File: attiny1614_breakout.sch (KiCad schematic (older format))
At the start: 15 parts, among them J1 Conn_01x07, J2 Conn_01x07, J3 UPDI, SW1 Reset, U1 REG102-5, U2 ATtiny1614-SS

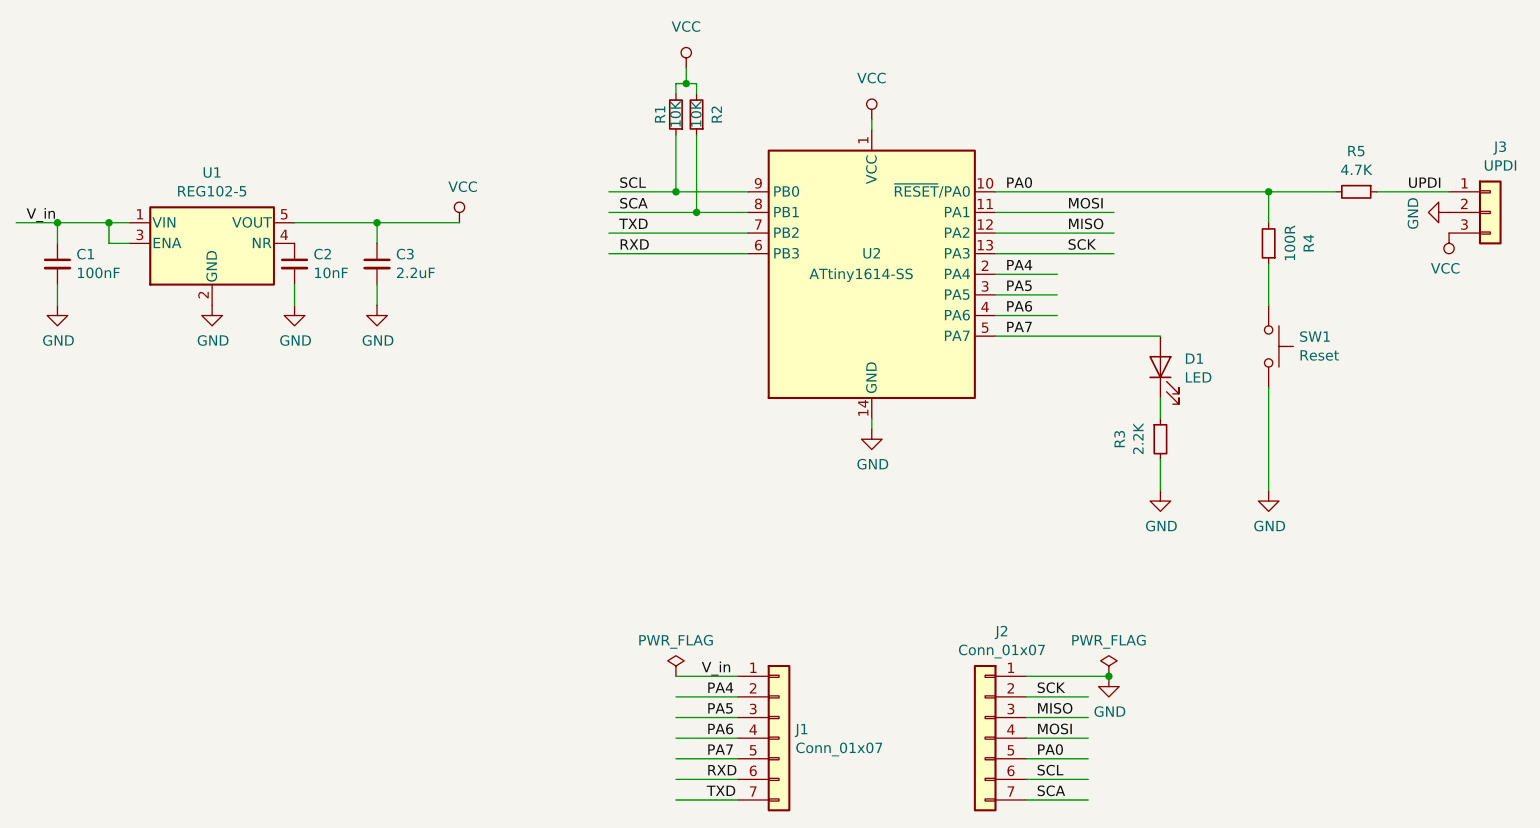
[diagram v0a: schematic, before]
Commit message: moved to programmer pin to Vin, fixed typos, added thermal relief
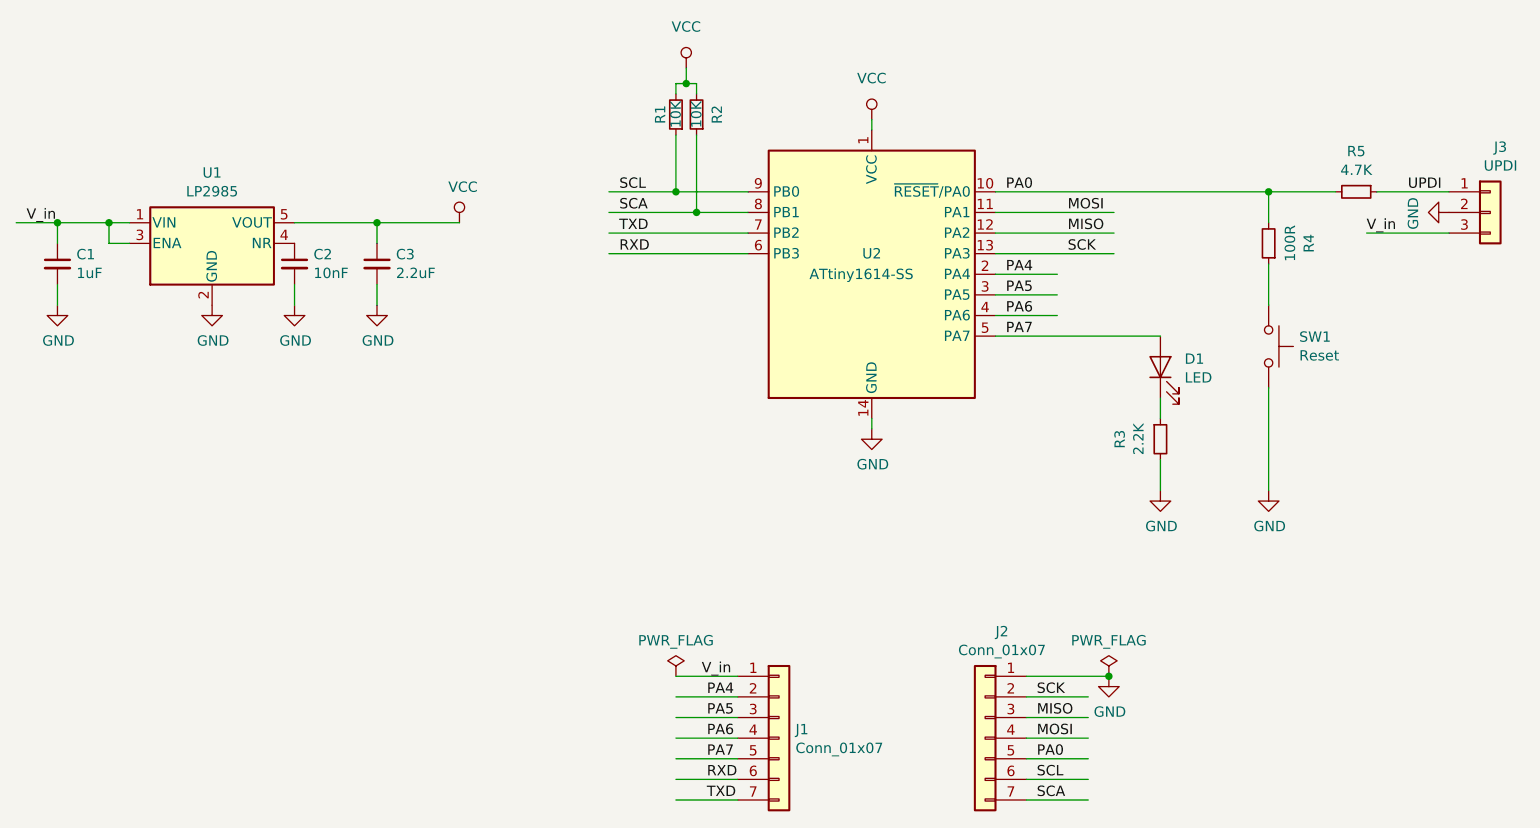
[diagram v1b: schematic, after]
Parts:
- C1: value 100nF -> 1uF
- U1: value REG102-5 -> LP2985
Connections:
- wire segments 56 -> 57
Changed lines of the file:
@@
 P 2250 2250
 F 0 "C1" H 2342 2296 50  0000 L CNN
-F 1 "100nF" H 2342 2205 50  0000 L CNN
+F 1 "1uF" H 2342 2205 50  0000 L CNN
 F 2 "Capacitor_SMD:C_0603_1608Metric_Pad1.05x0.95mm_HandSolder" H 2250 2250 50  0001 C CNN
 F 3 "~" H 2250 2250 50  0001 C CNN
@@
 $EndComp
 $Comp
-L power:VCC #PWR013
-U 1 1 5D418CA3
-P 9000 2100
-F 0 "#PWR013" H 9000 1950 50  0001 C CNN
-F 1 "VCC" H 9017 2273 50  0000 C CNN
-F 2 "" H 9000 2100 50  0001 C CNN
-F 3 "" H 9000 2100 50  0001 C CNN
-	1    9000 2100
-	-1   0    0    1
-$EndComp
-$Comp
 L power:GND #PWR08
 U 1 1 5D4188B9
@@
 P 3000 2150
 F 0 "U1" H 3000 2492 50  0000 C CNN
-F 1 "REG102-5" H 3000 2401 50  0000 C CNN
+F 1 "LP2985" H 3000 2401 50  0000 C CNN
 F 2 "Package_TO_SOT_SMD:SOT-23-5" H 3000 2475 50  0001 C CNN
 F 3 "http://www.ti.com/lit/ds/symlink/lp2985.pdf" H 3000 2150 50  0001 C CNN
@@
 Wire Wire Line
 	2250 2050 2500 2050
+Wire Wire Line
+	9000 2100 8600 2100
+Text Label 8600 2100 0    50   ~ 0
+V_in
 $EndSCHEMATC

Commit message: simplified power section
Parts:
- U1: symbol Regulator_Linear:REG102-5 -> attiny1614_breakout-rescue:REG102-5-Regulator_Linear
- U2: symbol MCU_Microchip_ATtiny:ATtiny1614-SS -> attiny1614_breakout-rescue:ATtiny1614-SS-MCU_Microchip_ATtiny
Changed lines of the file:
@@
 UPDI
 $Comp
-L MCU_Microchip_ATtiny:ATtiny1614-SS U2
+L attiny1614_breakout-rescue:ATtiny1614-SS-MCU_Microchip_ATtiny U2
 U 1 1 5D414195
 P 6200 2300
@@
 $EndComp
 $Comp
-L Regulator_Linear:REG102-5 U1
+L attiny1614_breakout-rescue:REG102-5-Regulator_Linear U1
 U 1 1 5D749571
 P 3000 2150

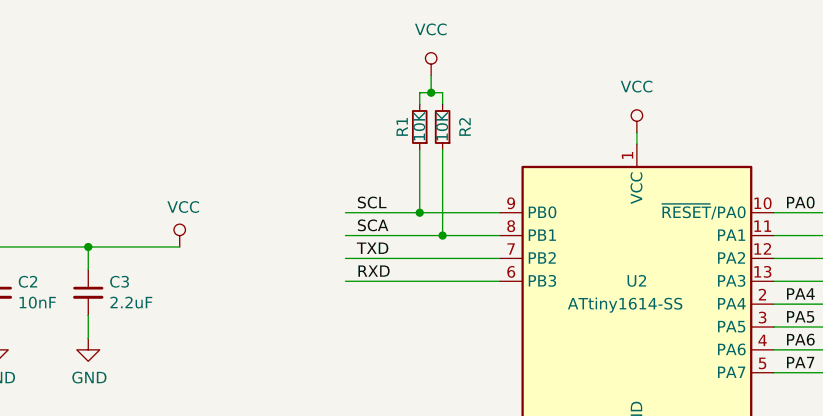
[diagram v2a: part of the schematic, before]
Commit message: changed VCC to 5V
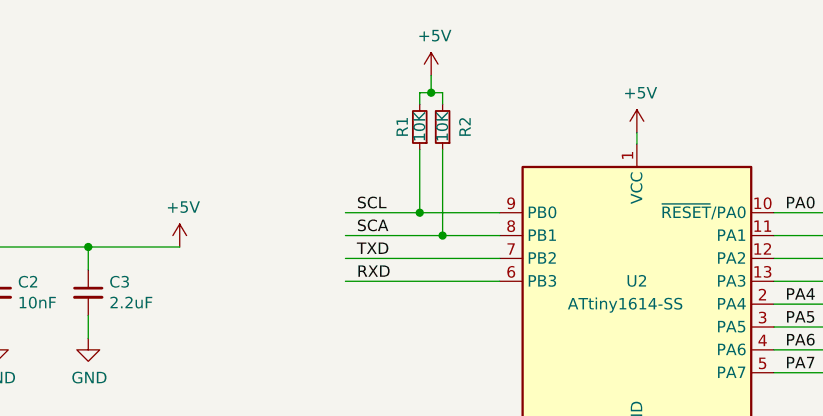
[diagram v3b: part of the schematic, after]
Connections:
- net labels added: +5V
- net labels removed: VCC
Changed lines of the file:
@@
-$EndComp
-$Comp
-L power:VCC #PWR05
-U 1 1 5D41B083
-P 4200 2050
-F 0 "#PWR05" H 4200 1900 50  0001 C CNN
-F 1 "VCC" H 4217 2223 50  0000 C CNN
-F 2 "" H 4200 2050 50  0001 C CNN
-F 3 "" H 4200 2050 50  0001 C CNN
-	1    4200 2050
-	1    0    0    -1
 $EndComp
 $Comp
@@
 $EndComp
 $Comp
-L power:VCC #PWR07
-U 1 1 5D41869F
-P 6200 1550
-F 0 "#PWR07" H 6200 1400 50  0001 C CNN
-F 1 "VCC" H 6200 1750 50  0000 C CNN
-F 2 "" H 6200 1550 50  0001 C CNN
-F 3 "" H 6200 1550 50  0001 C CNN
-	1    6200 1550
-	1    0    0    -1
-$EndComp
-$Comp
 L Connector_Generic:Conn_01x03 J3
 U 1 1 5D4170CD
@@
 Wire Wire Line
 	5250 1375 5250 1425
-$Comp
-L power:VCC #PWR06
-U 1 1 5D51D74C
-P 5300 1300
-F 0 "#PWR06" H 5300 1150 50  0001 C CNN
-F 1 "VCC" H 5300 1500 50  0000 C CNN
-F 2 "" H 5300 1300 50  0001 C CNN
-F 3 "" H 5300 1300 50  0001 C CNN
-	1    5300 1300
-	1    0    0    -1
-$EndComp
 Wire Wire Line
 	5300 1300 5300 1375
@@
 Text Label 8600 2100 0    50   ~ 0
 V_in
+$Comp
+L power:+5V #PWR?
+U 1 1 5EA06F55
+P 4200 2050
+F 0 "#PWR?" H 4200 1900 50  0001 C CNN
+F 1 "+5V" H 4215 2223 50  0000 C CNN
+F 2 "" H 4200 2050 50  0001 C CNN
+F 3 "" H 4200 2050 50  0001 C CNN
+	1    4200 2050
+	1    0    0    -1
+$EndComp
+$Comp
+L power:+5V #PWR?
+U 1 1 5EA0A404
+P 5300 1300
+F 0 "#PWR?" H 5300 1150 50  0001 C CNN
+F 1 "+5V" H 5315 1473 50  0000 C CNN
+F 2 "" H 5300 1300 50  0001 C CNN
+F 3 "" H 5300 1300 50  0001 C CNN
+	1    5300 1300
+	1    0    0    -1
+$EndComp
+$Comp
+L power:+5V #PWR?
+U 1 1 5EA0B8DE
+P 6200 1550
+F 0 "#PWR?" H 6200 1400 50  0001 C CNN
+F 1 "+5V" H 6215 1723 50  0000 C CNN
+F 2 "" H 6200 1550 50  0001 C CNN
+F 3 "" H 6200 1550 50  0001 C CNN
+	1    6200 1550
+	1    0    0    -1
+$EndComp
 $EndSCHEMATC
